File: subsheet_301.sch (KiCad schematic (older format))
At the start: 10 parts, among them J301 DB-19S ACSI Port, U302 74LS245_PHY, U306 74LS74_PHY, U307 74LS244_PHY

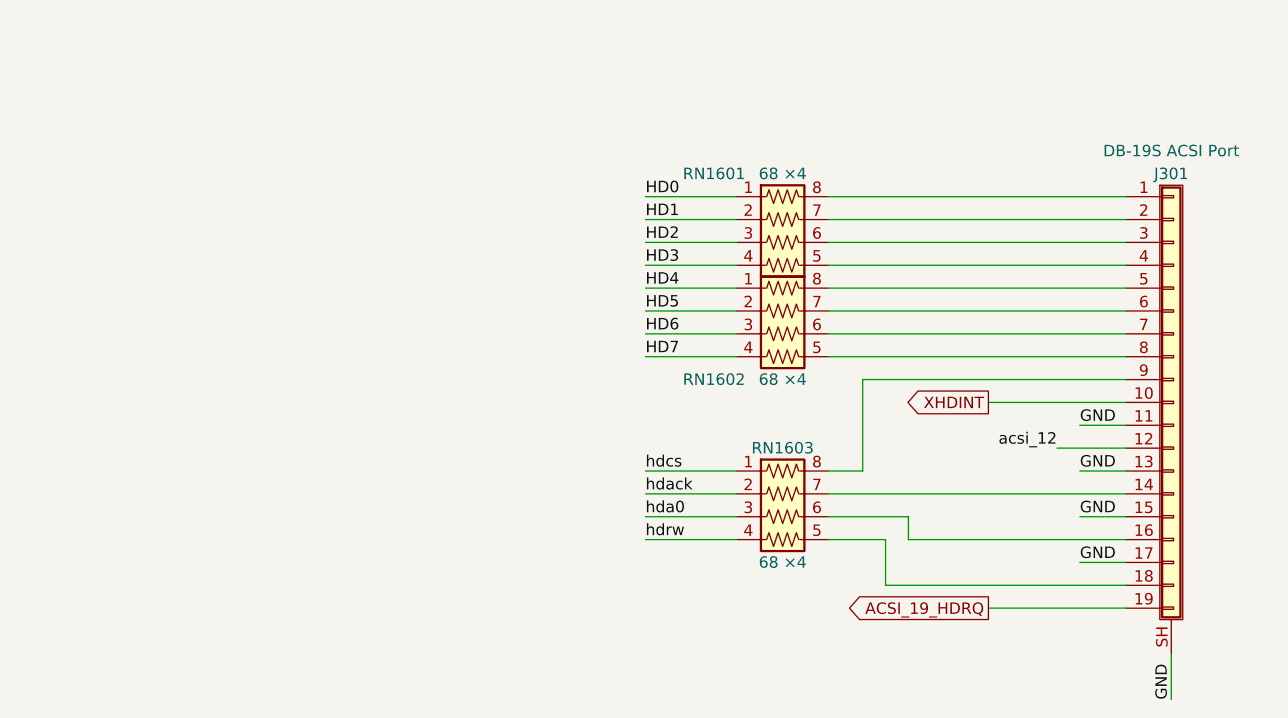
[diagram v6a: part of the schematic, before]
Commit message: Resolves #23 : Add internal ACSI port
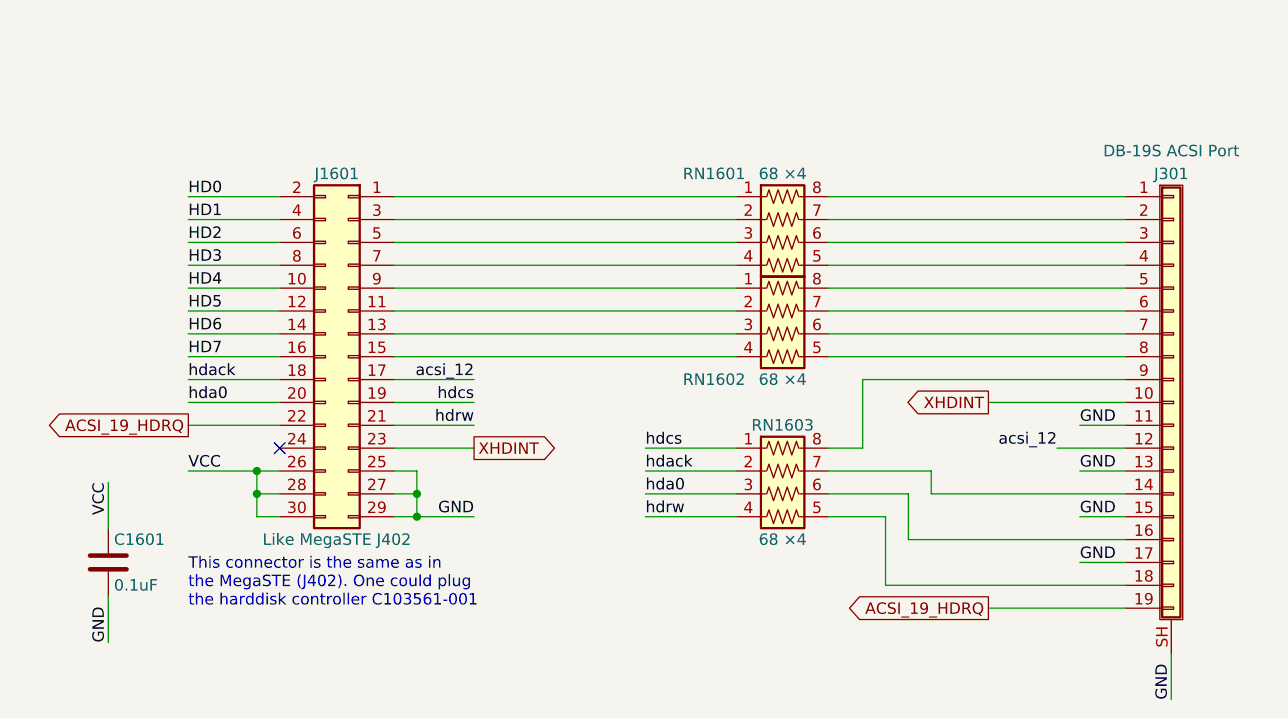
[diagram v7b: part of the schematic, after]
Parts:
- added C1601: 0.1uF, Capacitor_SMD:C_1206_3216Metric_Pad1.33x1.80mm_HandSolder, symbol Device:C
- added J1601: Like MegaSTE J402, Connector_PinHeader_2.54mm:PinHeader_2x15_P2.54mm_Vertical, symbol Connector_Generic:Conn_02x15_Odd_Even
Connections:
- net ACSI_19_HDRQ: now also J1601.22 (Pin_22)
- net GND: now also C1601.2, J1601.25 (Pin_25), J1601.27 (Pin_27), J1601.29 (Pin_29)
- net HD0: now also J1601.2 (Pin_2); no longer RN1601.1 (R1.1)
- net HD1: now also J1601.4 (Pin_4); no longer RN1601.2 (R2.1)
- net HD2: now also J1601.6 (Pin_6); no longer RN1601.3 (R3.1)
- net HD3: now also J1601.8 (Pin_8); no longer RN1601.4 (R4.1)
- net HD4: now also J1601.10 (Pin_10); no longer RN1602.1 (R1.1)
- net HD5: now also J1601.12 (Pin_12); no longer RN1602.2 (R2.1)
- net HD6: now also J1601.14 (Pin_14); no longer RN1602.3 (R3.1)
- net HD7: now also J1601.16 (Pin_16); no longer RN1602.4 (R4.1)
- net VCC: now also C1601.1, J1601.26 (Pin_26), J1601.28 (Pin_28), J1601.30 (Pin_30)
- net XHDINT: now also J1601.23 (Pin_23)
- net acsi_12: now also J1601.17 (Pin_17)
- net hda0: now also J1601.20 (Pin_20)
- net hdack: now also J1601.18 (Pin_18)
- net hdcs: now also J1601.19 (Pin_19)
- net hdrw: now also J1601.21 (Pin_21)
- new net: J1601.1 (Pin_1), RN1601.1 (R1.1)
- new net: J1601.3 (Pin_3), RN1601.2 (R2.1)
- new net: J1601.5 (Pin_5), RN1601.3 (R3.1)
- new net: J1601.7 (Pin_7), RN1601.4 (R4.1)
- new net: J1601.9 (Pin_9), RN1602.1 (R1.1)
- new net: J1601.11 (Pin_11), RN1602.2 (R2.1)
- new net: J1601.13 (Pin_13), RN1602.3 (R3.1)
- new net: J1601.15 (Pin_15), RN1602.4 (R4.1)
- no-connect marks 7 -> 8
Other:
- note added: "This connector is the same as in \nthe MegaSTE (J402). One could plug \nthe harddisk controller C103561-001"
- moved on the sheet: RN1603
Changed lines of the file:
@@
 	2250 5150 2250 5350
 Wire Wire Line
-	3350 6400 3750 6400
-Wire Wire Line
-	3350 6600 3750 6600
-Wire Wire Line
-	3350 6800 3750 6800
-Wire Wire Line
-	3350 7000 3750 7000
-Wire Wire Line
-	3350 7600 3750 7600
-Wire Wire Line
-	3350 7800 3750 7800
+	1350 6400 1750 6400
+Wire Wire Line
+	1350 6600 1750 6600
+Wire Wire Line
+	1350 6800 1750 6800
+Wire Wire Line
+	1350 7000 1750 7000
+Wire Wire Line
+	3350 7500 3750 7500
+Wire Wire Line
+	3350 7700 3750 7700
 $Comp
 L Connector_Generic_Shielded:Conn_01x19_Shielded J301
@@
 Text Label 3200 2400 2    50   ~ 0
 acsi_12
-Text Label 3350 6400 0    50   ~ 0
+Text Label 1350 6400 0    50   ~ 0
 HD0
-Text Label 3350 6500 0    50   ~ 0
+Text Label 1350 6500 0    50   ~ 0
 HD1
-Text Label 3350 6600 0    50   ~ 0
+Text Label 1350 6600 0    50   ~ 0
 HD2
-Text Label 3350 6700 0    50   ~ 0
+Text Label 1350 6700 0    50   ~ 0
 HD3
-Text Label 3350 6800 0    50   ~ 0
+Text Label 1350 6800 0    50   ~ 0
 HD4
-Text Label 3350 6900 0    50   ~ 0
+Text Label 1350 6900 0    50   ~ 0
 HD5
-Text Label 3350 7000 0    50   ~ 0
+Text Label 1350 7000 0    50   ~ 0
 HD6
-Text Label 3350 7100 0    50   ~ 0
+Text Label 1350 7100 0    50   ~ 0
 HD7
+Text Label 3350 7500 0    50   ~ 0
+hdcs
 Text Label 3350 7600 0    50   ~ 0
-hdcs
+hdack
 Text Label 3350 7700 0    50   ~ 0
-hdack
+hda0
 Text Label 3350 7800 0    50   ~ 0
-hda0
-Text Label 3350 7900 0    50   ~ 0
 hdrw
 Text Label 4800 2400 0    50   ~ 0
@@
 	4600 2500 5000 2500
 Wire Wire Line
-	3350 6500 3750 6500
-Wire Wire Line
-	3350 6700 3750 6700
-Wire Wire Line
-	3350 6900 3750 6900
-Wire Wire Line
-	3350 7100 3750 7100
+	1350 6500 1750 6500
+Wire Wire Line
+	1350 6700 1750 6700
+Wire Wire Line
+	1350 6900 1750 6900
+Wire Wire Line
+	1350 7100 1750 7100
 Text Label 5650 8600 1    50   ~ 0
 GND
@@
 L custom_passives:R_Pack04_US RN1603
 U 1 1 61FF4DF9
-P 3950 7800
-F 0 "RN1603" V 3650 7800 50  0000 C CNN
-F 1 "68 ×4" V 4150 7800 50  0000 C CNN
-F 2 "Resistor_SMD:R_Array_Convex_4x0603" V 4225 7800 50  0001 C CNN
-F 3 "~" H 3950 7800 50  0001 C CNN
-	1    3950 7800
+P 3950 7700
+F 0 "RN1603" V 3650 7700 50  0000 C CNN
+F 1 "68 ×4" V 4150 7700 50  0000 C CNN
+F 2 "Resistor_SMD:R_Array_Convex_4x0603" V 4225 7700 50  0001 C CNN
+F 3 "~" H 3950 7700 50  0001 C CNN
+	1    3950 7700
 	0    1    1    0
 $EndComp
@@
 	4150 7100 5450 7100
 Wire Wire Line
-	3350 7700 3750 7700
-Wire Wire Line
-	3350 7900 3750 7900
-Wire Wire Line
-	4150 7700 5450 7700
-Wire Wire Line
-	4150 7900 4400 7900
-Wire Wire Line
-	4400 7900 4400 8100
+	3350 7600 3750 7600
+Wire Wire Line
+	3350 7800 3750 7800
 Wire Wire Line
 	4400 8100 5450 8100
 Wire Wire Line
-	4150 7800 4500 7800
-Wire Wire Line
-	4500 7800 4500 7900
-Wire Wire Line
 	4500 7900 5450 7900
 Wire Wire Line
-	4150 7600 4300 7600
-Wire Wire Line
-	4300 7600 4300 7200
+	4150 7500 4300 7500
 Wire Wire Line
 	4300 7200 5450 7200
@@
 Wire Wire Line
 	4150 6700 5450 6700
+$Comp
+L Connector_Generic:Conn_02x15_Odd_Even J1601
+U 1 1 6299D251
+P 2050 7100
+F 0 "J1601" H 2100 7900 50  0000 C CNN
+F 1 "Like MegaSTE J402" H 2100 6300 50  0000 C CNN
+F 2 "Connector_PinHeader_2.54mm:PinHeader_2x15_P2.54mm_Vertical" H 2050 7100 50  0001 C CNN
+F 3 "~" H 2050 7100 50  0001 C CNN
+	1    2050 7100
+	-1   0    0    -1
+$EndComp
+Wire Wire Line
+	4150 7600 4600 7600
+Wire Wire Line
+	5450 7700 4600 7700
+Wire Wire Line
+	4600 7700 4600 7600
+Wire Wire Line
+	4300 7500 4300 7200
+Wire Wire Line
+	4150 7700 4500 7700
+Wire Wire Line
+	4500 7700 4500 7900
+Wire Wire Line
+	4150 7800 4400 7800
+Wire Wire Line
+	4400 7800 4400 8100
+Text Label 1350 7200 0    50   ~ 0
+hdack
+Wire Wire Line
+	1350 7200 1750 7200
+Wire Wire Line
+	1350 7300 1750 7300
+Text Label 1350 7300 0    50   ~ 0
+hda0
+Text GLabel 1350 7400 0    50   Output ~ 0
+ACSI_19_HDRQ
+NoConn ~ 1750 7500
+$Comp
+L Device:C C?
+U 1 1 62A0B5E0
+P 1000 8000
+AR Path="/60786F27/6078774E/62A0B5E0" Ref="C?"  Part="1"
+AR Path="/60786F27/607875AF/62A0B5E0" Ref="C?"  Part="1"
+AR Path="/6089D0BA/62A0B5E0" Ref="C?"  Part="1"
+AR Path="/608A2359/62A0B5E0" Ref="C?"  Part="1"
+AR Path="/60A1445F/62A0B5E0" Ref="C?"  Part="1"
+AR Path="/60A73CDE/62A0B5E0" Ref="C1601"  Part="1"
+F 0 "C1601" H 1025 8100 50  0000 L CNN
+F 1 "0.1uF" H 1025 7900 50  0000 L CNN
+F 2 "Capacitor_SMD:C_1206_3216Metric_Pad1.33x1.80mm_HandSolder" H 1038 7850 50  0001 C CNN
+F 3 "~" H 1000 8000 50  0001 C CNN
+	1    1000 8000
+	1    0    0    -1
+$EndComp
+Text Label 1000 8350 1    50   ~ 0
+GND
+Text Label 1000 7650 3    50   ~ 0
+VCC
+Wire Wire Line
+	1000 8150 1000 8350
+Wire Wire Line
+	1750 7700 1650 7700
+Wire Wire Line
+	1650 7700 1650 7600
+Wire Wire Line
+	1650 7600 1750 7600
+Wire Wire Line
+	1750 7800 1650 7800
+Wire Wire Line
+	1650 7800 1650 7700
+Connection ~ 1650 7700
+Text Label 2600 7800 2    50   ~ 0
+GND
+Wire Wire Line
+	2250 7600 2350 7600
+Wire Wire Line
+	2350 7600 2350 7700
+Wire Wire Line
+	2250 7700 2350 7700
+Connection ~ 2350 7700
+Wire Wire Line
+	2350 7700 2350 7800
+Wire Wire Line
+	2250 7800 2350 7800
+Connection ~ 2350 7800
+Text Label 1350 7600 0    50   ~ 0
+VCC
+Wire Wire Line
+	1350 7600 1650 7600
+Connection ~ 1650 7600
+Wire Wire Line
+	1000 7650 1000 7850
+Text Label 2600 7200 2    50   ~ 0
+acsi_12
+Wire Wire Line
+	2600 7200 2250 7200
+Wire Wire Line
+	2350 7800 2600 7800
+Text Label 2600 7300 2    50   ~ 0
+hdcs
+Text Label 2600 7400 2    50   ~ 0
+hdrw
+Text GLabel 2600 7500 2    50   Output ~ 0
+XHDINT
+Wire Wire Line
+	2250 7300 2600 7300
+Wire Wire Line
+	2600 7400 2250 7400
+Wire Wire Line
+	2250 7500 2600 7500
+Wire Wire Line
+	1350 7400 1750 7400
+Wire Wire Line
+	2250 6400 3750 6400
+Wire Wire Line
+	2250 6500 3750 6500
+Wire Wire Line
+	2250 6600 3750 6600
+Wire Wire Line
+	2250 6700 3750 6700
+Wire Wire Line
+	2250 6800 3750 6800
+Wire Wire Line
+	2250 6900 3750 6900
+Wire Wire Line
+	2250 7000 3750 7000
+Wire Wire Line
+	2250 7100 3750 7100
+Text Notes 1350 8200 0    50   ~ 0
+This connector is the same as in \nthe MegaSTE (J402). One could plug \nthe harddisk controller C103561-001
 $EndSCHEMATC
